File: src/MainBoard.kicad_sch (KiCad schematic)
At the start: 79 parts, among them J1 MiniFit_2x05_F, J10 Conn_01x01, J11 Conn_01x01, J12 Conn_01x01, J13 Conn_01x01, J14 Conn_01x01, J15 Conn_01x01, J16 Conn_01x01, J17 Conn_01x01, J18 Conn_01x01, J19 Conn_01x01, J2 MiniFit_2x05_F, J20 Conn_01x01, J21 Conn_01x01, J22 Conn_01x01, J24 Conn_01x01, J25 Conn_01x01, J3 Conn_01x01, J4 Conn_01x01, J5 Conn_01x01, J6 Conn_01x01, J7 Conn_01x01, J8 Conn_01x01, J9 Conn_01x01, K1 RAYEX-L90, K2 LEG-12, K3 LEG-12, Q1 2N7002, Q2 2N7002, Q3 2N7002, Q4 2N7002, Q5 2N7002, Q6 2N7002, SW1 SW_SPST

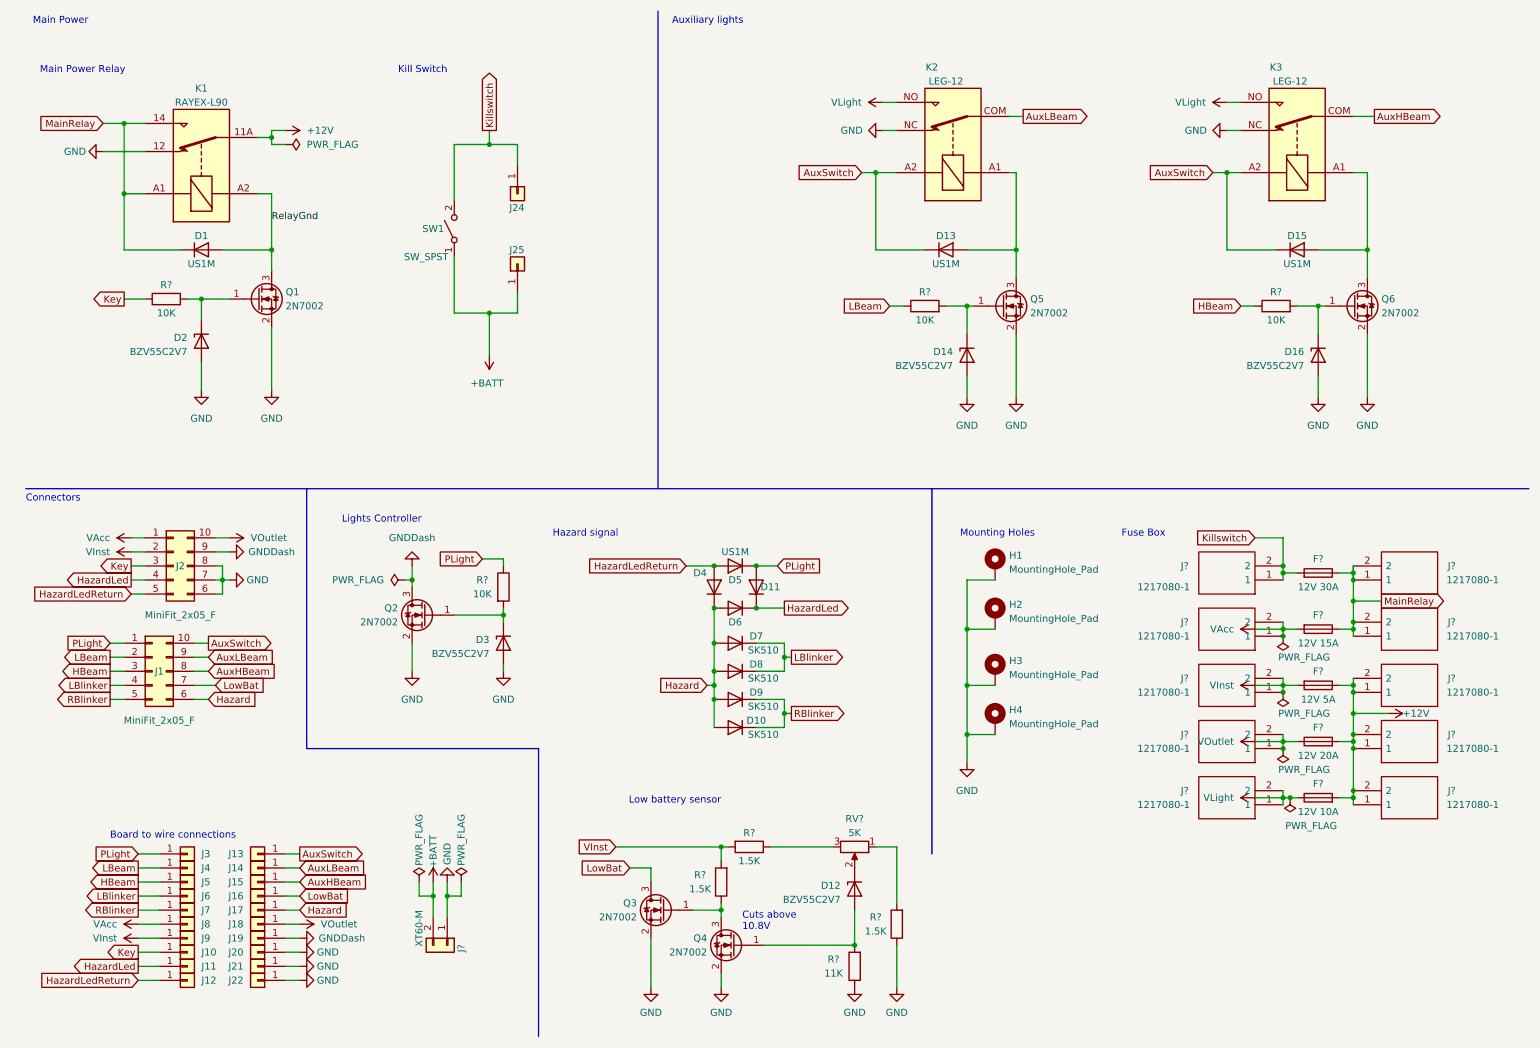
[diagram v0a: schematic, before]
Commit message: Fix battery sensor
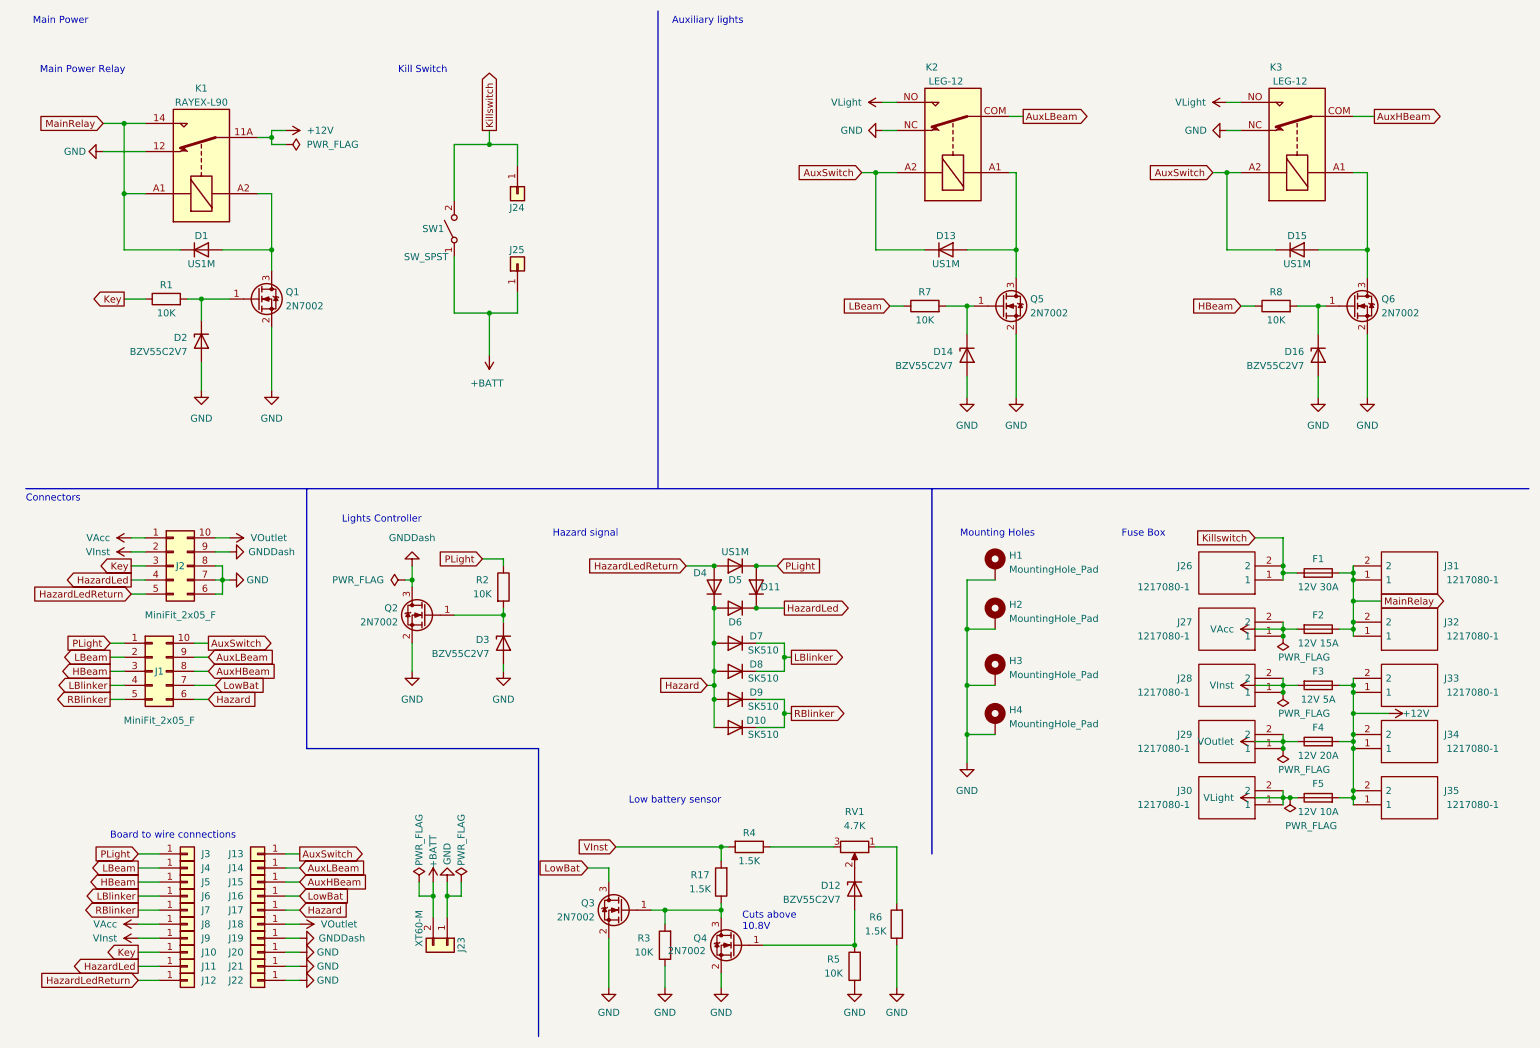
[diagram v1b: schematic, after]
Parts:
- added R17: 1.5K, Resistor_SMD:R_1206_3216Metric_Pad1.30x1.75mm_HandSolder, symbol Device:R
- R3: renamed from R?; value 1.5K -> 10K
- R5: renamed from R?; value 11K -> 10K
- RV1: renamed from RV?; value 5K -> 4.7K
- gave numbers to parts that had none: 22
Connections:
- net GND: now also R3.1
- net VInst: now also R17.2; no longer R3.2
- net at Q3.1 (G), Q4.3 (D): now also R3.2, R17.1; no longer R3.1
- net RelayGnd: no longer names the net of D1.2 (A), K1.A2, Q1.3 (D)
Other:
- moved on the sheet: Q3, R3

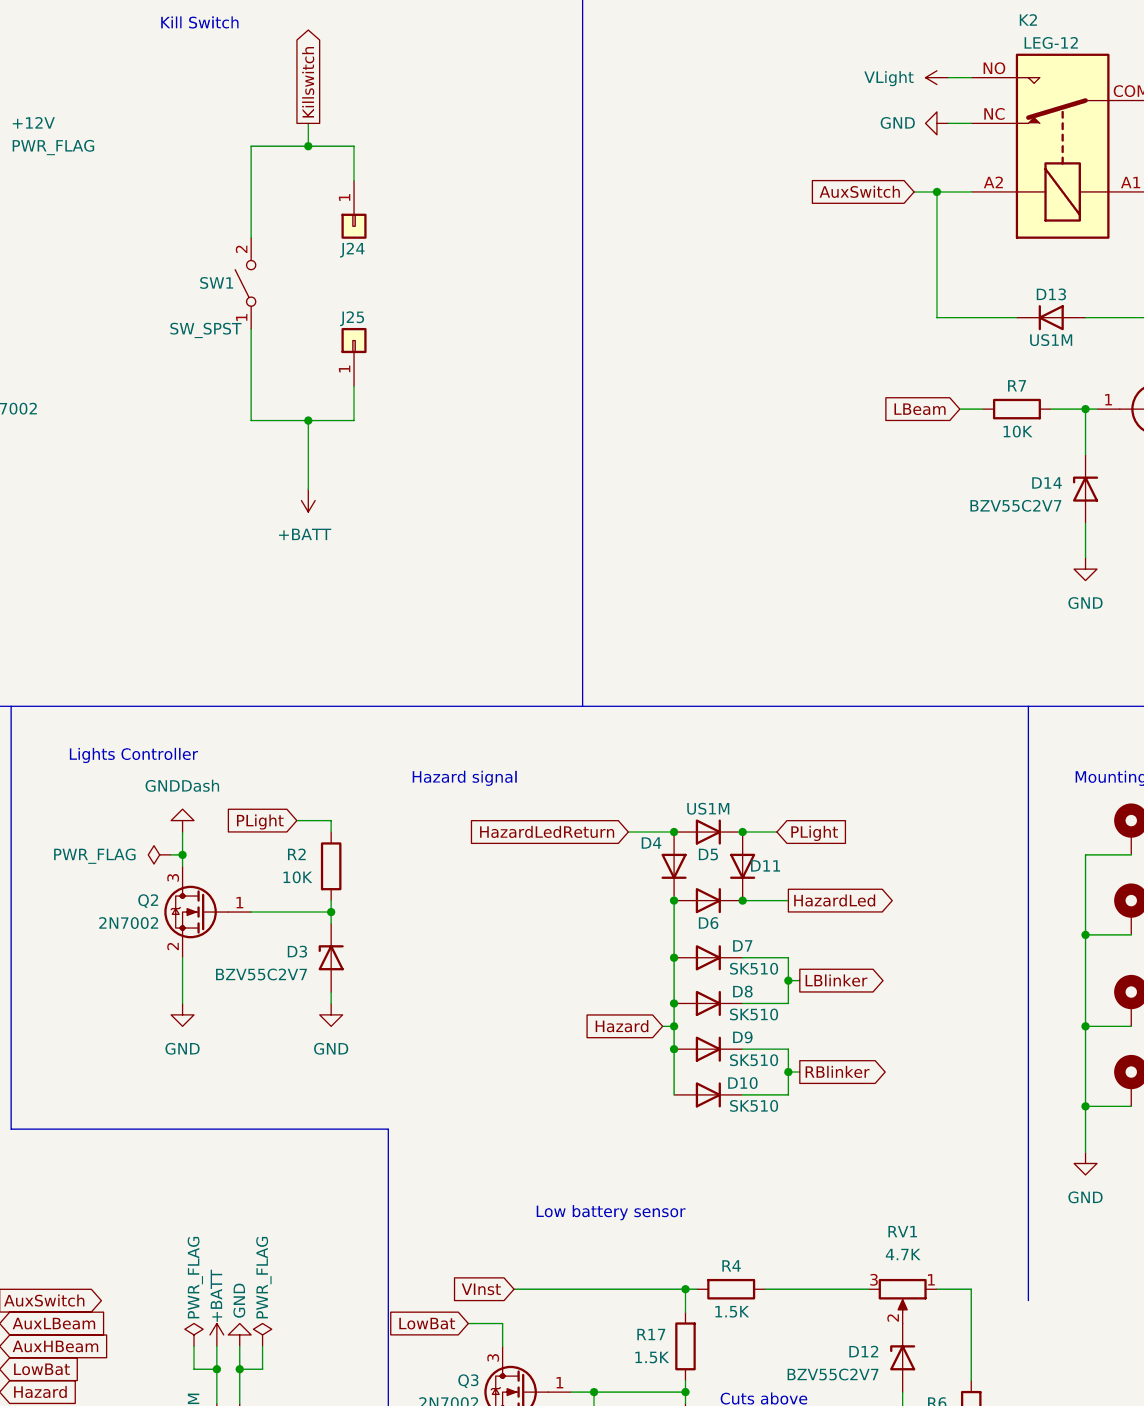
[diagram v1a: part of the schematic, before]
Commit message: Add LED Blinkers balasts; Update PCB
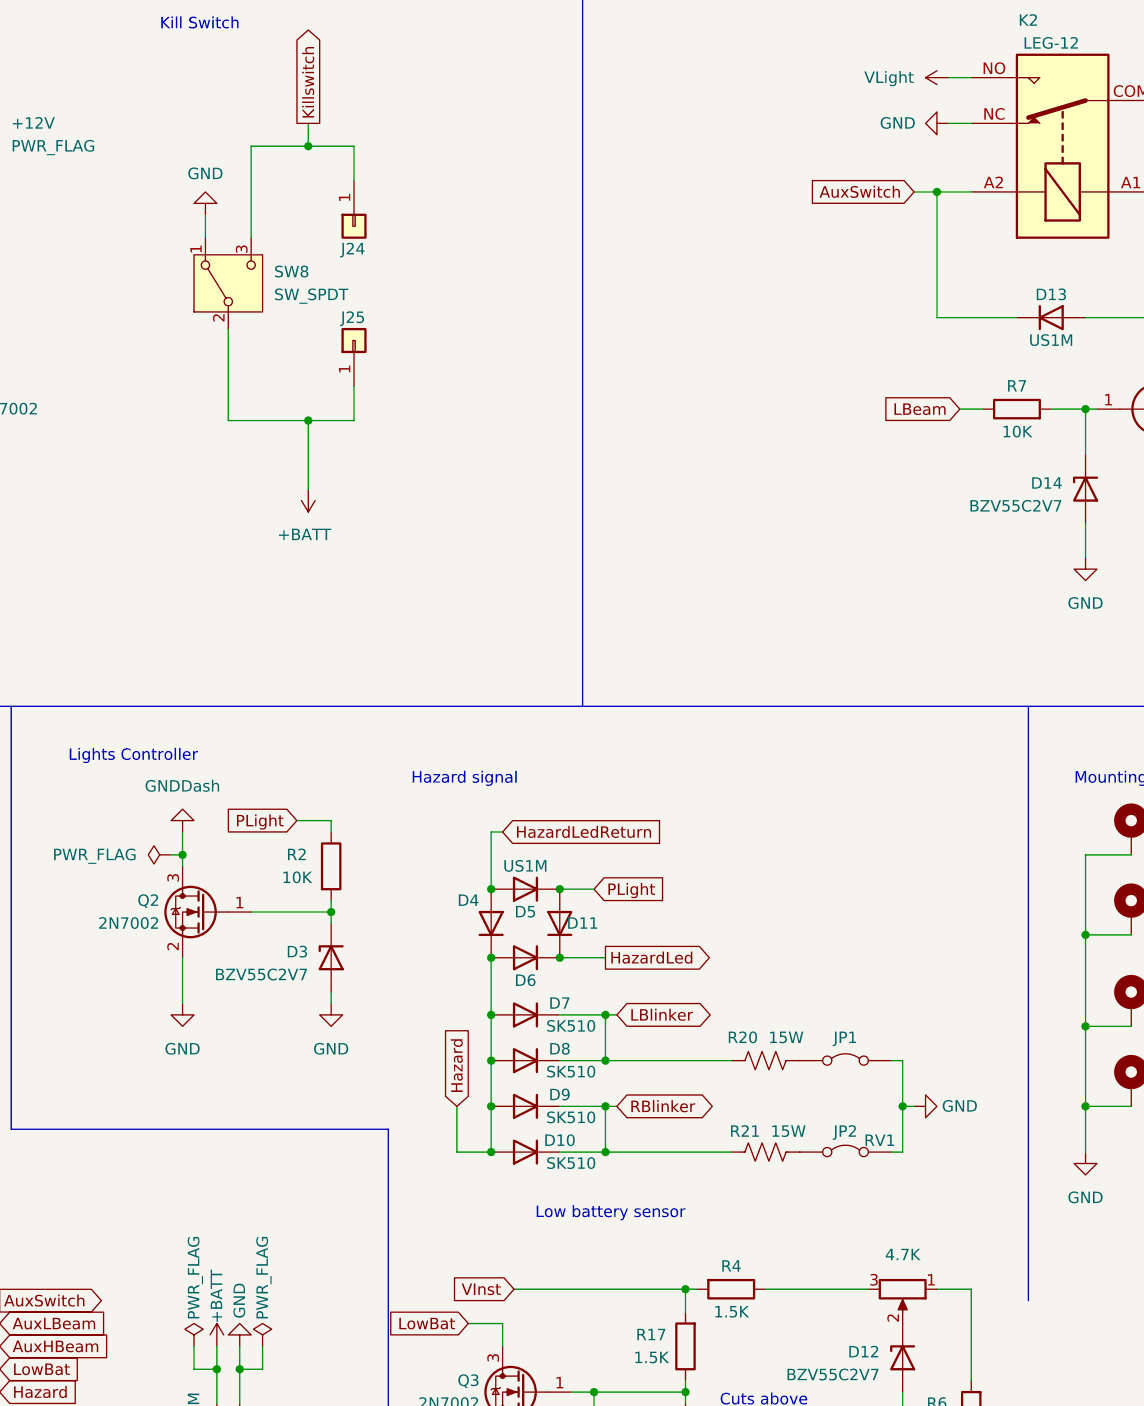
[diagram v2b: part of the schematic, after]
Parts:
- removed SW1: SW_SPST, symbol Switch:SW_SPST
- added JP1, JP2: Jumper_2_Bridged, Connector_PinHeader_2.54mm:PinHeader_1x02_P2.54mm_Vertical, symbol Jumper:Jumper_2_Bridged
- added R20, R21: 15W, Resistor_THT:R_Axial_Power_L60.0mm_W14.0mm_P66.04mm, symbol Device:R_US
- added SW8: SW_SPDT, symbol Switch:SW_SPDT
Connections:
- net +BATT: now also SW8.2 (B)
- net GND: now also JP1.2 (B), JP2.2 (B), SW8.1 (A)
- net Killswitch: now also SW8.3 (C)
- net LBlinker: now also R20.1
- net RBlinker: now also R21.1
- new net: JP1.1 (A), R20.2
- new net: JP2.1 (A), R21.2
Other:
- moved on the sheet: D10, D11, D4, D5, D6, D7, D8, D9
